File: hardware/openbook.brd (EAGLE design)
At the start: 170.2 x 111.2 mm, 103 parts, among them IC1 XC6220A331MR-G, IC2 BD5229G-TR, J1 SAMACSYS_PARTS_USB4110-GF-A, J2 112A-TAAR-R03_ATTEND, J3 QWIIC_RIGHT_ANGLE, J4 FH34SRJ-24S-0.5SH_99_, Q1 20V/4.2A/52mΩ/1.4W, Q2 20V/4.2A/52mΩ/1.4W, Q3 20V/4.2A/52mΩ/1.4W, U1 ESP32-C6-WROOM-1-N8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

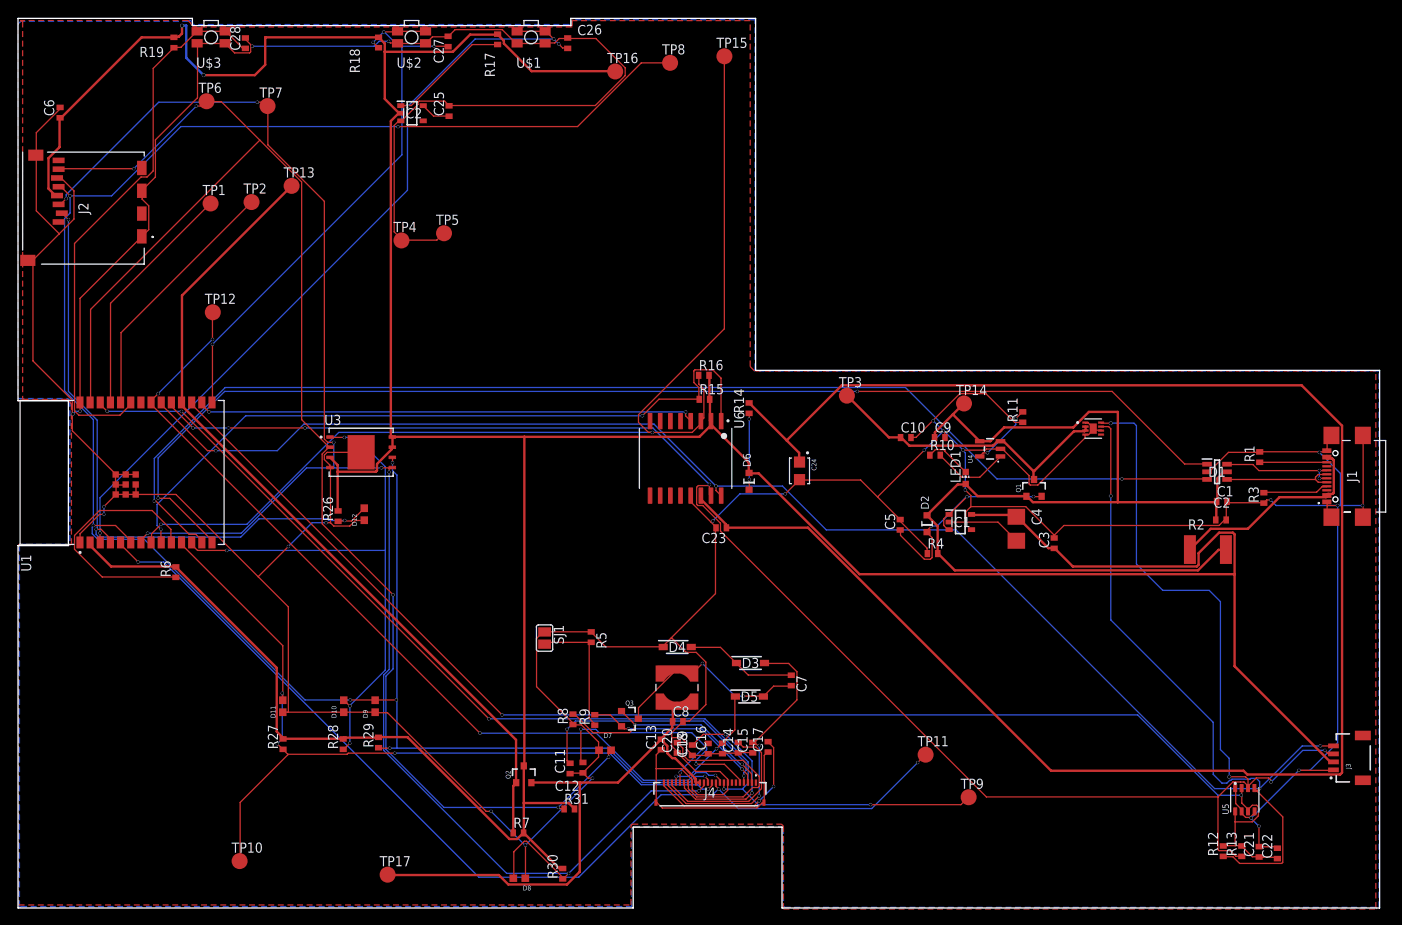
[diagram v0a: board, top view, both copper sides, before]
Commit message: Updated button positions, wire angles, allignment
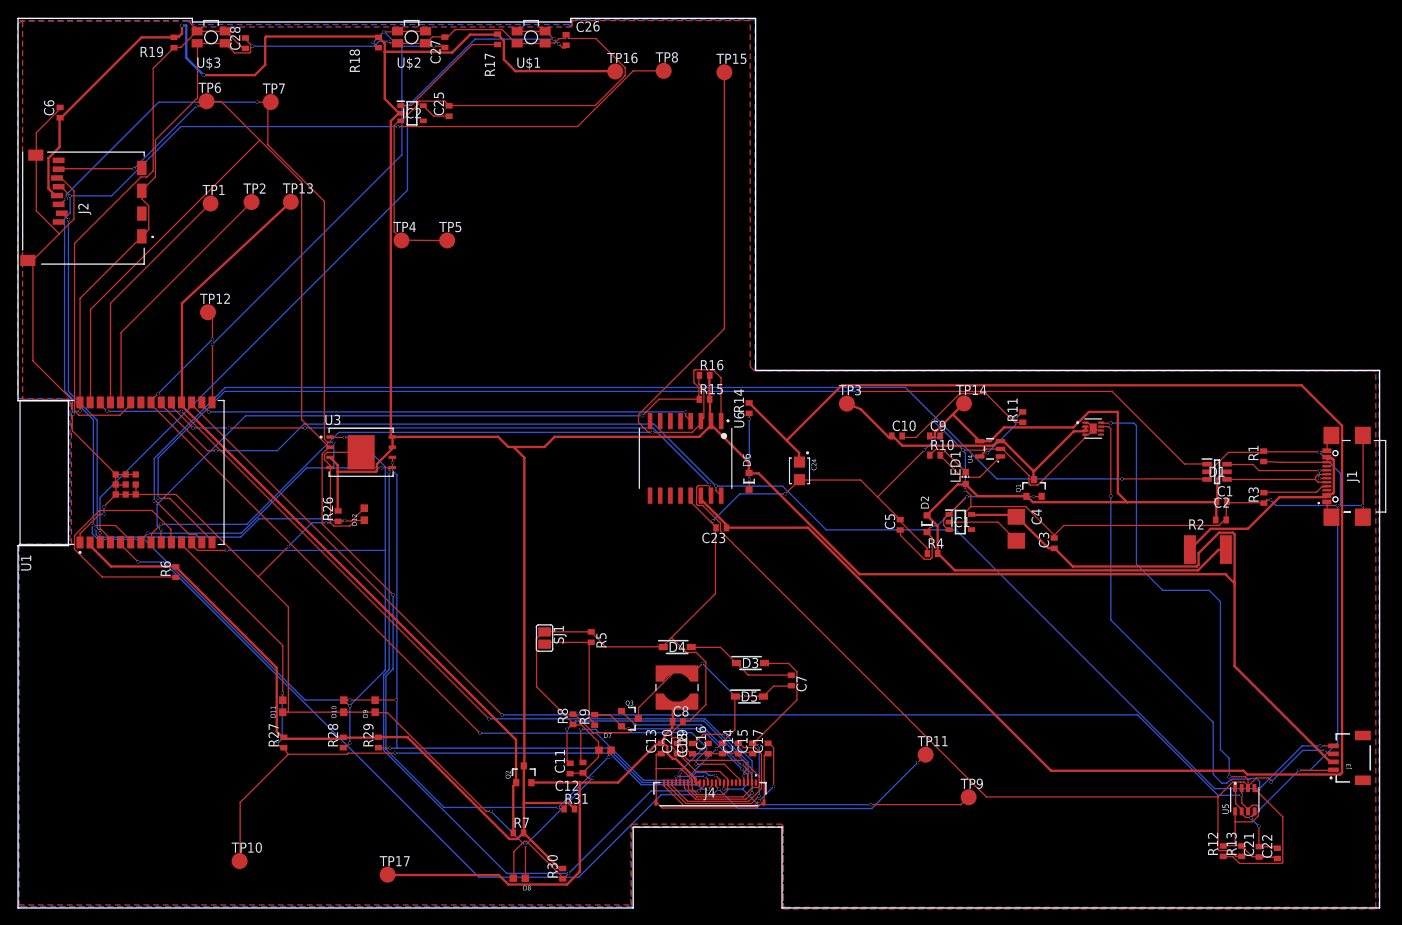
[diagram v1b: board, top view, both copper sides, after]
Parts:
- moved TP13 2.00 mm to (28.7, 5.06)
- moved TP15 2.00 mm to (82.9, 21.3)
- moved TP8 1.28 mm to (75.3, 21.4)
- moved C10 1.12 mm to (104.5, -24.2)
- moved TP3 1.00 mm to (98.2, -20.2)
- moved TP5 0.98 mm to (48.2, 0.24)
- moved TP7 0.64 mm to (26.2, 17.5)
- moved C9 0.63 mm to (109.2, -24.2)
- moved TP12 0.60 mm to (18.4, -8.74)
- moved R1 0.51 mm to (150.3, -26.7)
- moved C13 0.50 mm to (75.0, -63.3)
- moved C26 0.45 mm to (63.1, 25.3)
- moved C27 0.41 mm to (48.0, 25.0)
- moved R27 0.22 mm to (27.8, -62.5)
- moved C17 0.20 mm to (88.4, -63.3)
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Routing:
- net 3V3: track 497.1 -> 499.3 mm
- net INT_RTC: track 134.4 -> 132.5 mm
- net EPD_3V3_C: track 104.0 -> 102.3 mm
- net GND: track 783.4 -> 784.7 mm
- net SCK: track 260.7 -> 259.5 mm
- net VBUS: track 129.6 -> 130.7 mm
- net MOSI: track 217.0 -> 218.0 mm
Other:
- outline, holes or cut-outs redrawn

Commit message: Fixed ground plane and silkscreen issues
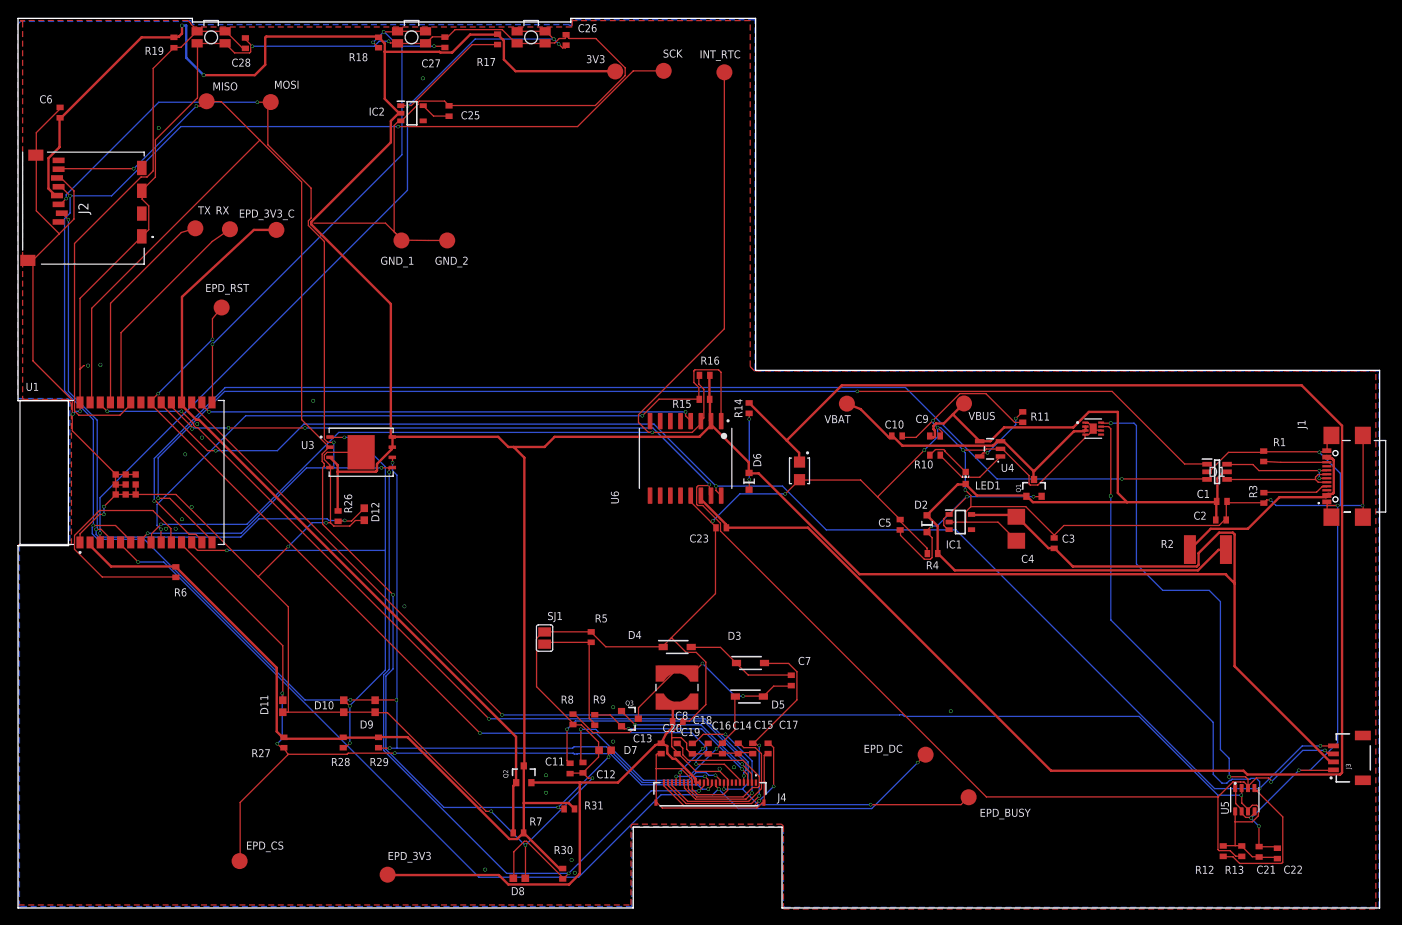
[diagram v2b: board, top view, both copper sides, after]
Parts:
- moved TP2 4.34 mm to (21.1, 1.64)
- moved TP13 3.94 mm to (26.9, 1.56)
- moved TP1 3.64 mm to (16.8, 1.76)
- moved TP12 1.80 mm to (20.1, -8.14)
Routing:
- net GND: track 784.7 -> 798.2 mm, vias 25 -> 48
- net 3V3: track 499.3 -> 507.5 mm
- net RX: track 31.8 -> 27.6 mm
- net TX: track 30.1 -> 26.7 mm
- net EPD_3V3_C: track 102.3 -> 99.8 mm
- net EPD_RST: track 106.6 -> 107.4 mm
- net VBUS: track 130.7 -> 131.4 mm
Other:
- board text added: "3V3"
- board text added: "EPD_3V3"
- board text added: "EPD_3V3_C"
- board text added: "EPD_BUSY"
- board text added: "EPD_CS"
- board text added: "EPD_DC"
- board text added: "EPD_RST"
- board text added: "GND_1"
- board text added: "GND_2"
- board text added: "INT_RTC"
- board text added: "MISO"
- board text added: "MOSI"
- board text added: "RX"
- board text added: "SCK"
- board text added: "TX"
- board text added: "VBAT"
- board text added: "VBUS"
